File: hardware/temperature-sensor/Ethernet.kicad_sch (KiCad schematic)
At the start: 2 parts, among them J1 1881626, U2 LAN8720A

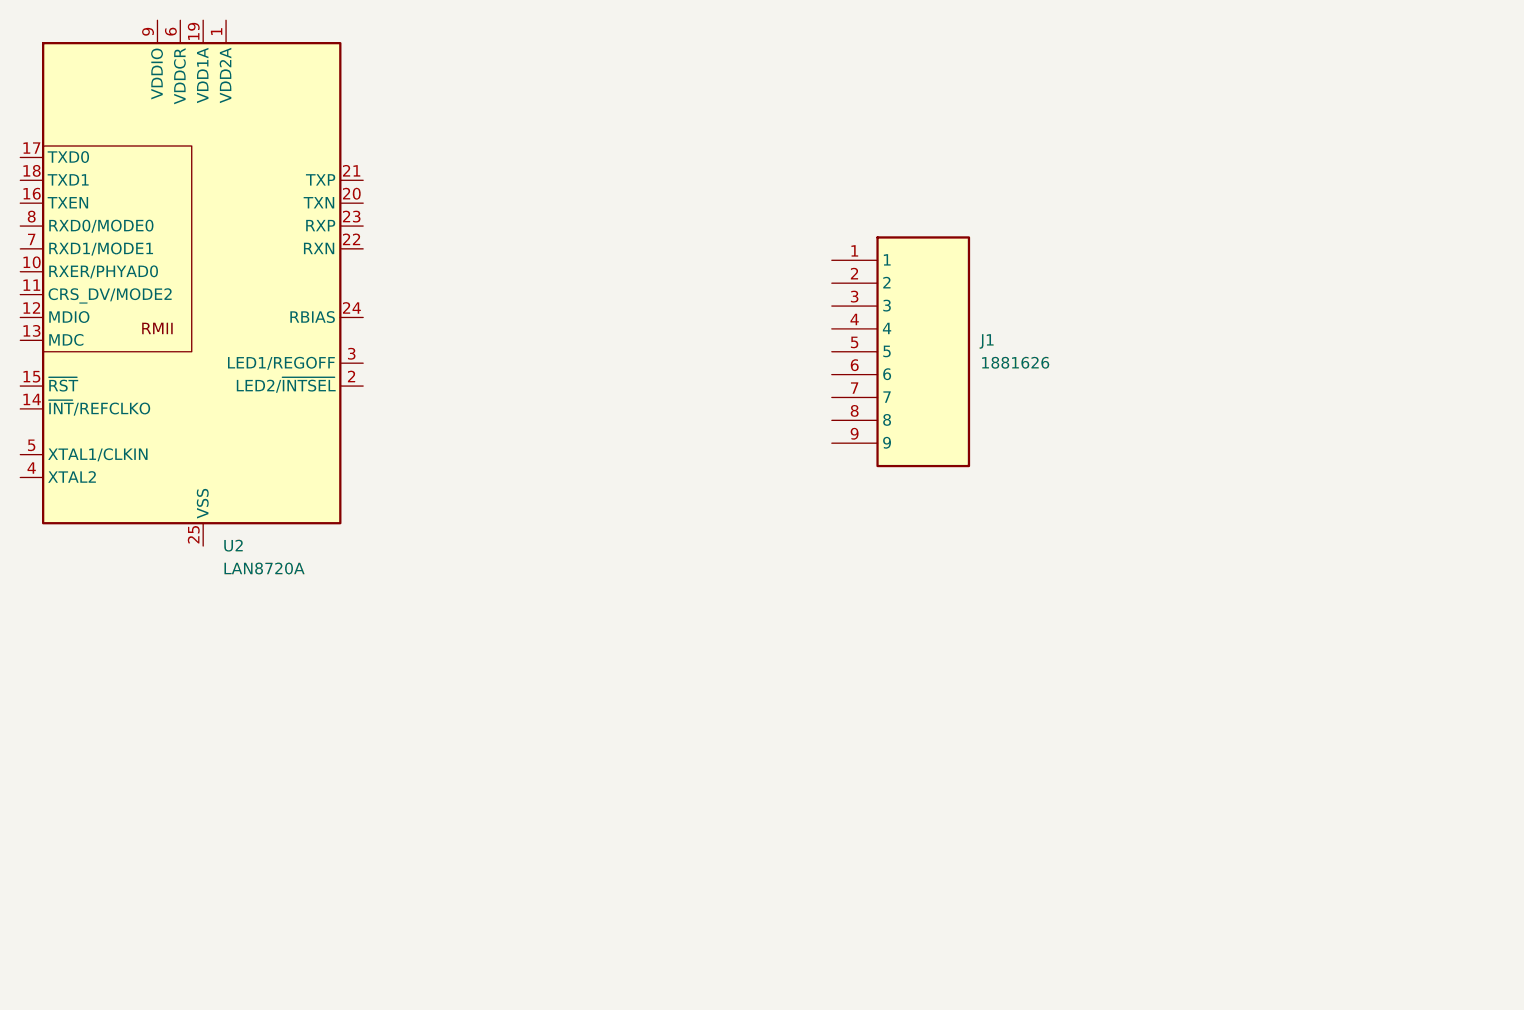
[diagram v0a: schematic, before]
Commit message: add components for temperature sensor
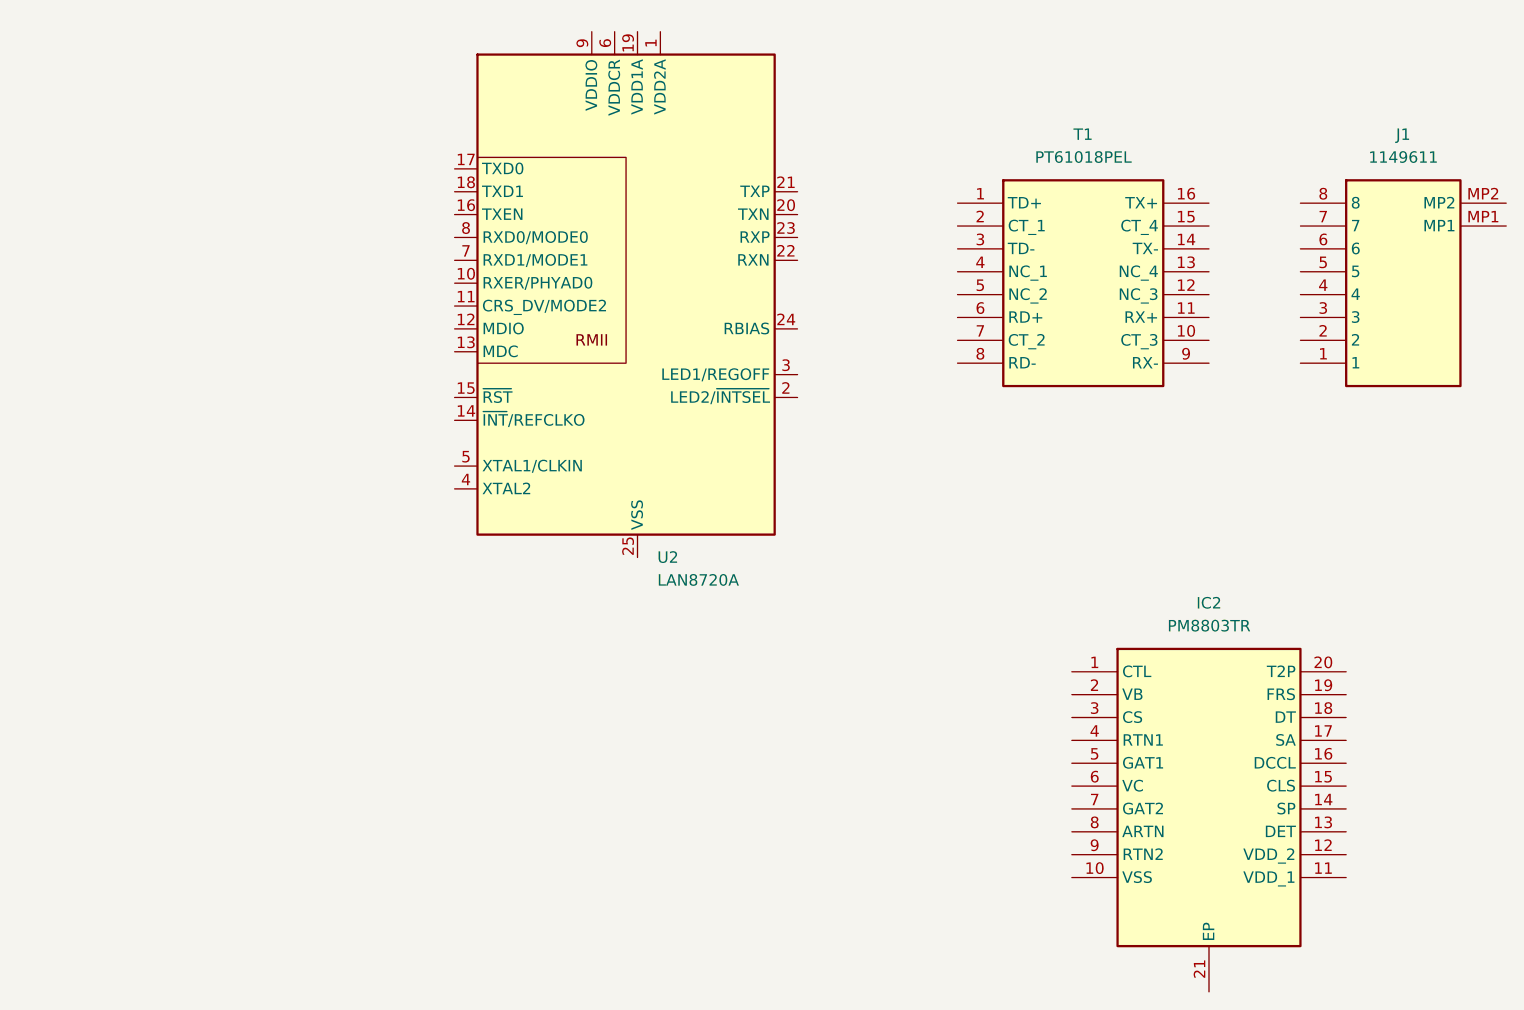
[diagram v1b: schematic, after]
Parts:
- removed J1: 1881626, benediktibk:phoenix_contact_1881626, symbol benediktibk:phoenix_contact_1881626
- added IC2: PM8803TR, benediktibk:SOP65P640X120-21N, symbol benediktibk:PM8803TR
- added J1: 1149611, benediktibk:1149611, symbol benediktibk:1149611
- added T1: PT61018PEL, benediktibk:SOIC127P930X565-16N, symbol benediktibk:PT61018PEL
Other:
- moved on the sheet: U2

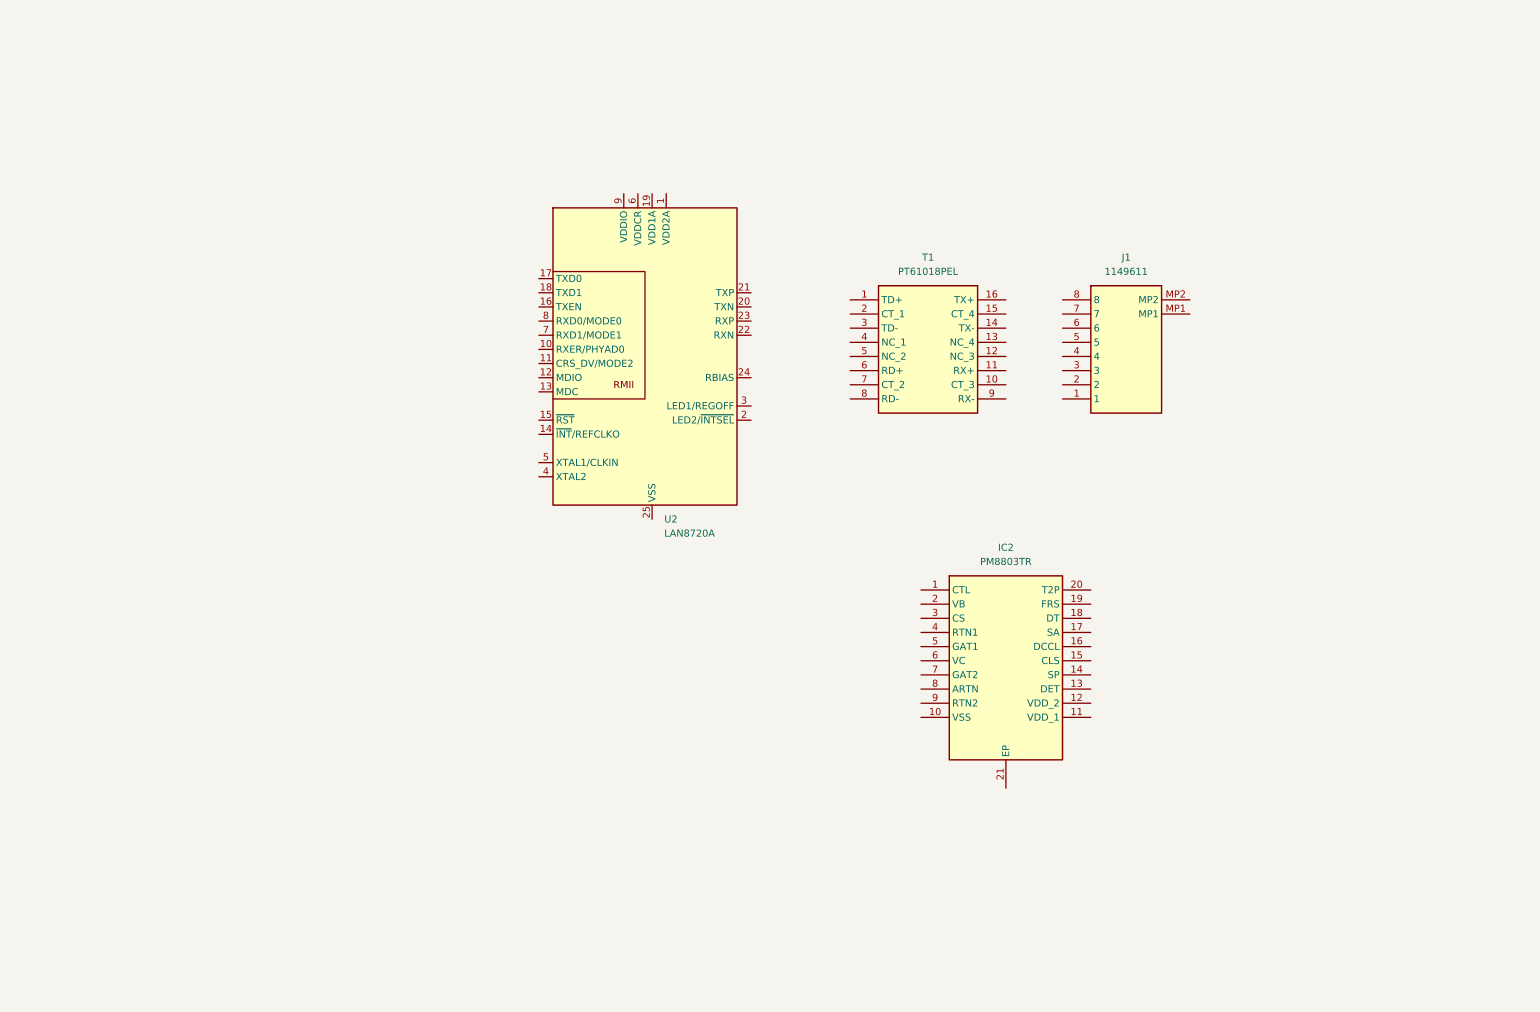
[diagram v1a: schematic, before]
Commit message: extend schematic of ethernet
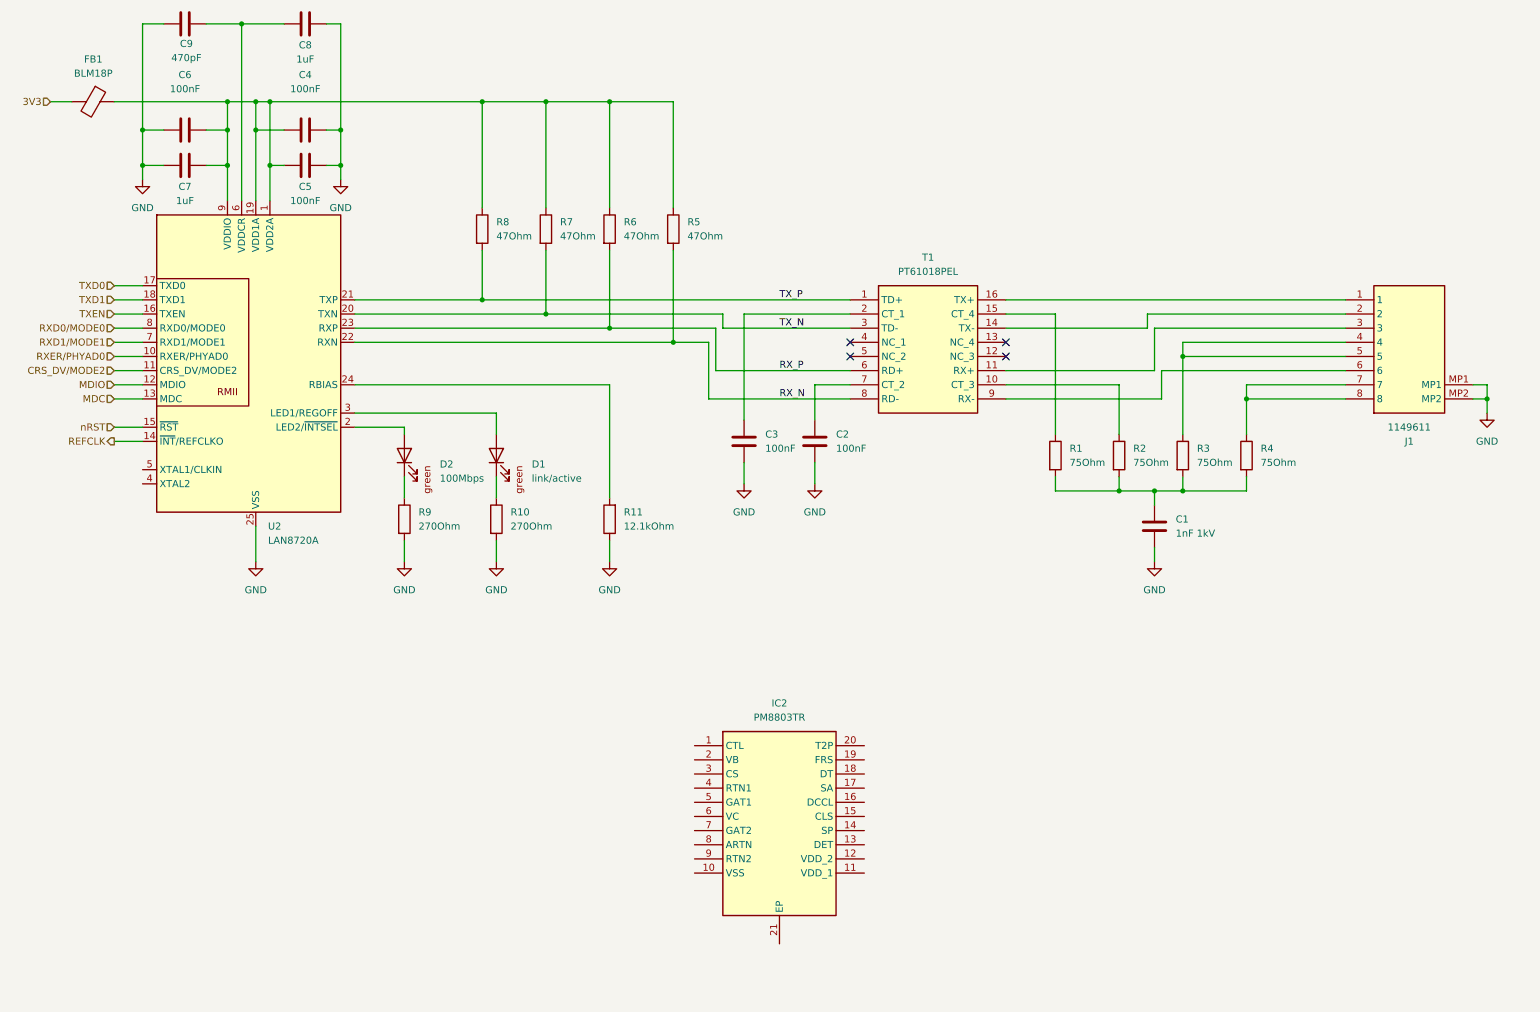
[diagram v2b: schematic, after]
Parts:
- added C1: 1nF 1kV, benediktibk:C_0603_1608Metric_Pad1.08x0.95mm_HandSolder, symbol benediktibk:C_1nF_SMD_0603_1000V_10%
- added C2, C3, C4, C5, C6: 100nF, benediktibk:C_0603_1608Metric_Pad1.08x0.95mm_HandSolder, symbol benediktibk:C_100nF_SMD_0603_50V
- added C7, C8: 1uF, benediktibk:C_0603_1608Metric_Pad1.08x0.95mm_HandSolder, symbol benediktibk:C_1uF_SMD_0603_50V_10%
- added C9: 470pF, benediktibk:C_0603_1608Metric_Pad1.08x0.95mm_HandSolder, symbol benediktibk:C_470pF_SMD_0603_50V_5%
- added D1: link/active, benediktibk:D_0603_1608Metric_Pad1.05x0.95mm_HandSolder, symbol benediktibk:LED_green_0603
- added D2: 100Mbps, benediktibk:D_0603_1608Metric_Pad1.05x0.95mm_HandSolder, symbol benediktibk:LED_green_0603
- added FB1: BLM18P, benediktibk:R_0603_1608Metric_Pad0.98x0.95mm_HandSolder, symbol benediktibk:BLM18P
- added R1, R2, R3, R4: 75Ohm, benediktibk:R_0603_1608Metric_Pad0.98x0.95mm_HandSolder, symbol benediktibk:R_75Ohm_SMD_0603_100mW_1%
- added R10, R9: 270Ohm, benediktibk:R_0603_1608Metric_Pad0.98x0.95mm_HandSolder, symbol benediktibk:R_270Ohm_SMD_0603_100mW_1%
- added R11: 12.1kOhm, benediktibk:R_0603_1608Metric_Pad0.98x0.95mm_HandSolder, symbol benediktibk:R_12_1kOhm_SMD_0603_100mW_1%
- added R5, R6, R7, R8: 47Ohm, benediktibk:R_0603_1608Metric_Pad0.98x0.95mm_HandSolder, symbol benediktibk:R_47Ohm_SMD_0603_100mW_1%
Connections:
- net TX_P: now reaches T1.1 (TD+)
- net TX_P: now also U2.21 (TXP), R8.2
- net at T1.10 (CT_3): now also R2.1
- net at T1.11 (RX+): now also J1.3
- net at T1.14 (TX-): now also J1.2
- net at T1.15 (CT_4): now also R1.1
- net at T1.16 (TX+): now also J1.1
- net at T1.2 (CT_1): now also C3.1
- net TX_N: now reaches T1.3 (TD-)
- net TX_N: now also U2.20 (TXN), R7.2
- net RX_P: now reaches T1.6 (RD+)
- net RX_P: now also U2.23 (RXP), R6.2
- net at T1.7 (CT_2): now also C2.1
- net RX_N: now reaches T1.8 (RD-)
- net RX_N: now also U2.22 (RXN), R5.2
- net at T1.9 (RX-): now also J1.6
- net at U2.1 (VDD2A): now also U2.19 (VDD1A), U2.9 (VDDIO), C4.2, C5.1, C6.1, C7.1, FB1.1, R5.1, R6.1, R7.1, R8.1
- net RXER/PHYAD0: now reaches U2.10 (RXER/PHYAD0)
- net CRS_DV/MODE2: now reaches U2.11 (CRS_DV/MODE2)
- net MDIO: now reaches U2.12 (MDIO)
- net MDC: now reaches U2.13 (MDC)
- net REFCLK: now reaches U2.14 (~{INT}/REFCLKO)
- net nRST: now reaches U2.15 (~{RST})
- net TXEN: now reaches U2.16 (TXEN)
- net TXD0: now reaches U2.17 (TXD0)
- net TXD1: now reaches U2.18 (TXD1)
- net at U2.2 (LED2/~{INTSEL}): now also D2.2 (A)
- net at U2.24 (RBIAS): now also R11.2
- net GND: now reaches U2.25 (VSS)
- net GND: now also J1.MP1, J1.MP2, C1.2, C2.2, C3.2, C4.1, C5.2, C6.2, C7.2, C8.1, C9.2, R10.2, R11.1, R9.2
- net at U2.3 (LED1/REGOFF): now also D1.2 (A)
- net at U2.6 (VDDCR): now also C8.2, C9.1
- net RXD1/MODE1: now reaches U2.7 (RXD1/MODE1)
- net RXD0/MODE0: now reaches U2.8 (RXD0/MODE0)
- net at J1.4: now also J1.5, R3.1
- net at J1.7: now also J1.8, R4.1
- new net: C1.1, R1.2, R2.2, R3.2, R4.2
- new net: D2.1 (K), R9.1
- new net: D1.1 (K), R10.1
- new net 3V3: FB1.2
- no-connect marks 0 -> 4
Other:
- moved on the sheet: IC2, J1, U2

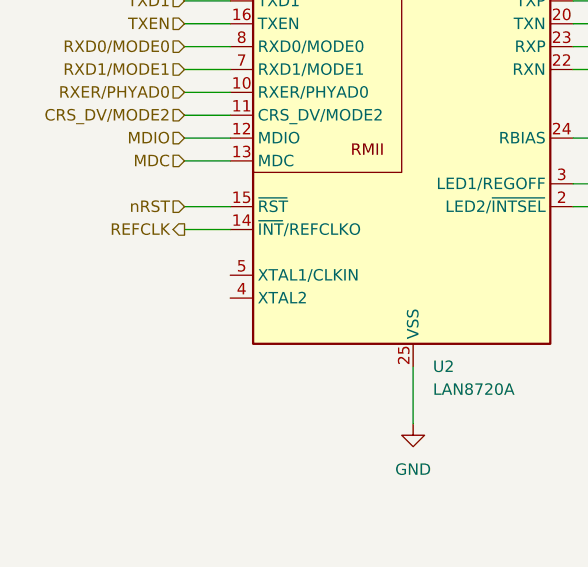
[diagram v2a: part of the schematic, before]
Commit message: add quartz
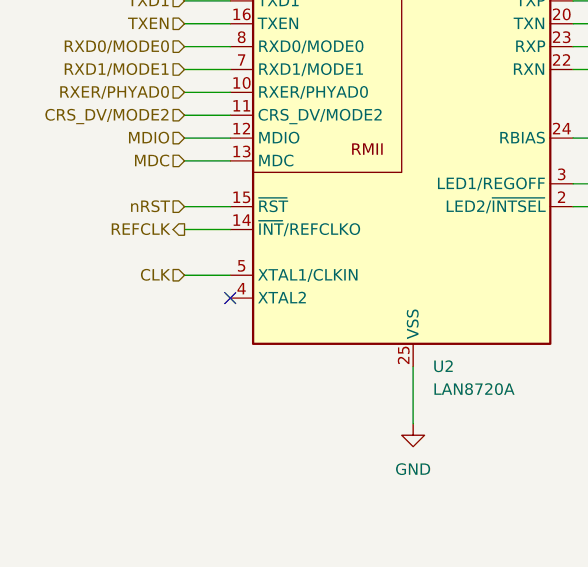
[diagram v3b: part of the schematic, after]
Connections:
- net CLK: now reaches U2.5 (XTAL1/CLKIN)
- no-connect marks 4 -> 5
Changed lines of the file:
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@@
+	)
+	(no_connect
+		(at 34.29 97.79)
 	)
 	(no_connect
@@
 		(pts
 			(xy 29.21 64.77) (xy 34.29 64.77)
+		)
+		(stroke
+			(width 0)
+			(type default)
+		)
+	)
+	(wire
+		(pts
+			(xy 29.21 95.25) (xy 34.29 95.25)
 		)
 		(stroke
@@
 		)
 	)
+	(hierarchical_label "CLK"
+		(shape input)
+		(at 29.21 95.25 180)
+		(effects
+			(font
+				(size 1.27 1.27)
+			)
+			(justify right)
+		)
+	)
